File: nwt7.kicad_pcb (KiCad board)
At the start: 2 copper layers, 119.1 x 117.3 mm, 128 parts, among them IC1 PIC16F876A, IC10 AD8307, IC11 MSA0886, IC12 78L10, IC13 AP1117D50, IC15 AP1117D50, IC16 AD8361, IC2 MAX232, IC4 AP1117D50, IC5 AP1117D50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

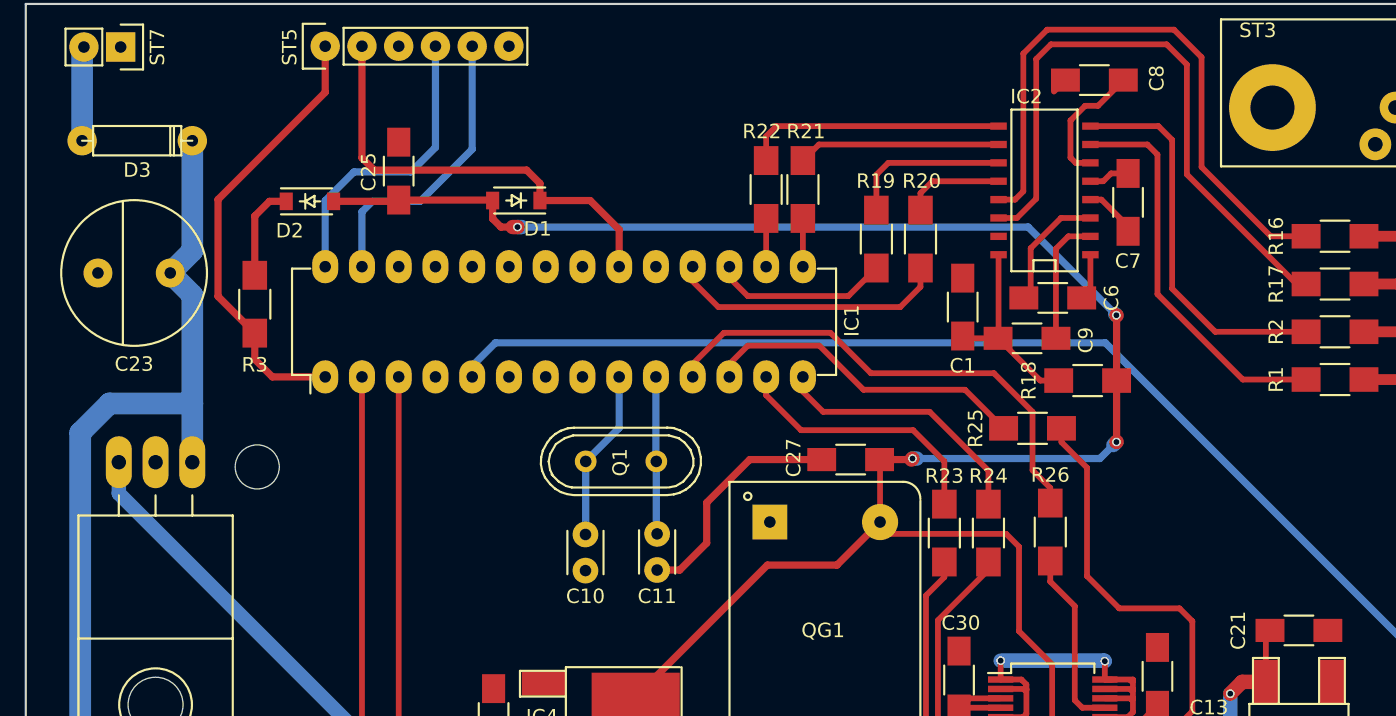
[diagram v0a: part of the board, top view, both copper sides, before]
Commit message: fixed IC3 power
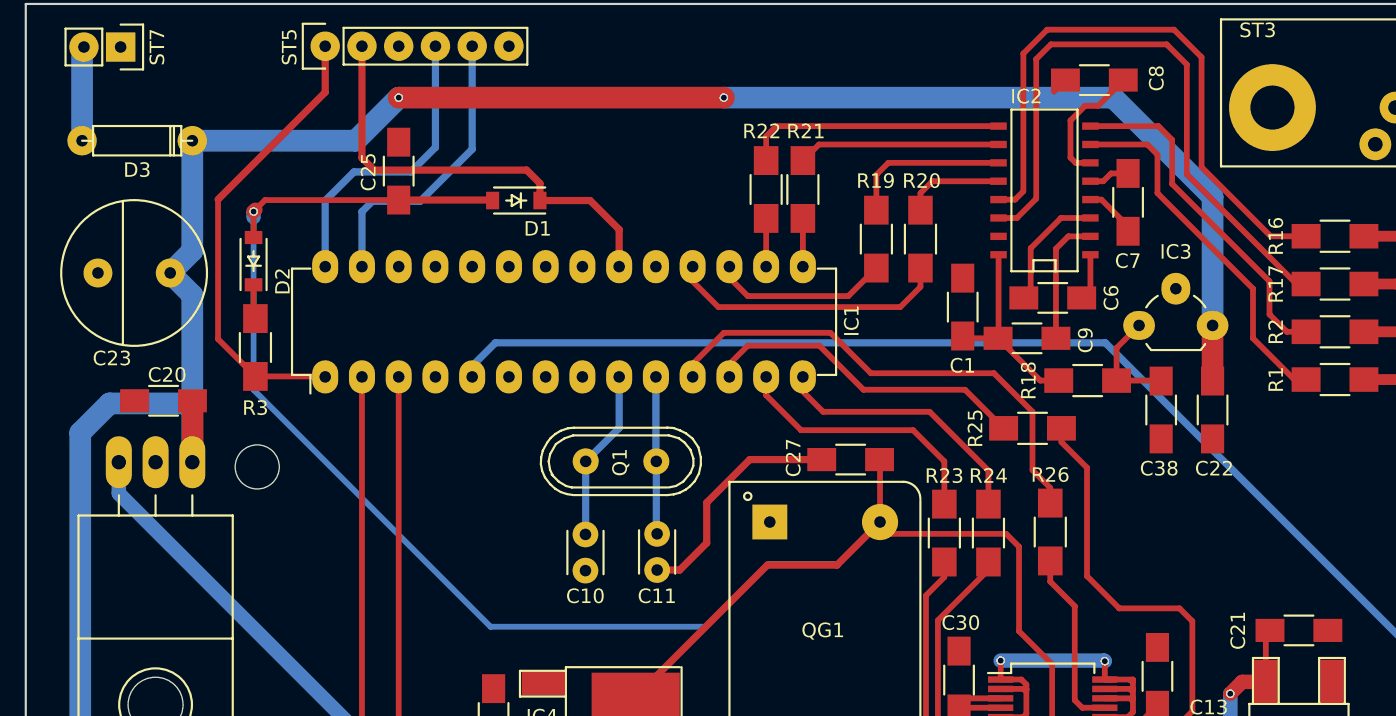
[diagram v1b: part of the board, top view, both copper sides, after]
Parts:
- added C20: 10u, Capacitors_SMD:C_1206_HandSoldering, F.Cu at (21.6, 39.5)
- added C22: 100n, Capacitors_SMD:C_1206_HandSoldering, F.Cu at (94.1, 40.1)
- added C38: 100n, Capacitors_SMD:C_1206_HandSoldering, F.Cu at (90.6, 40.1)
- added IC3: 78L05, TO_SOT_Packages_THT:TO-92_Rugged, F.Cu at (89.0, 34.3)
- moved D2 5.68 mm to (27.8, 29.8), turned to 90 degrees
- moved R3 2.99 mm to (27.9, 35.8)
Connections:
- R18 pad 2: Net-(C25-Pad1) -> Net-(C38-Pad2)
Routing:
- net Net-(C2-Pad2): track 173.7 -> 265.3 mm, vias 0 -> 2
- net Net-(C38-Pad2): track 0.00 -> 7.55 mm
- net Net-(D2-Pad1): track 6.69 -> 2.45 mm
- net Net-(IC2-Pad8): track 26.8 -> 23.9 mm
- net Net-(IC2-Pad7): track 27.3 -> 25.2 mm
- net Net-(IC1-Pad1): track 31.1 -> 31.8 mm
- net Net-(C25-Pad1): track 156.0 -> 156.4 mm, vias 4 -> 1

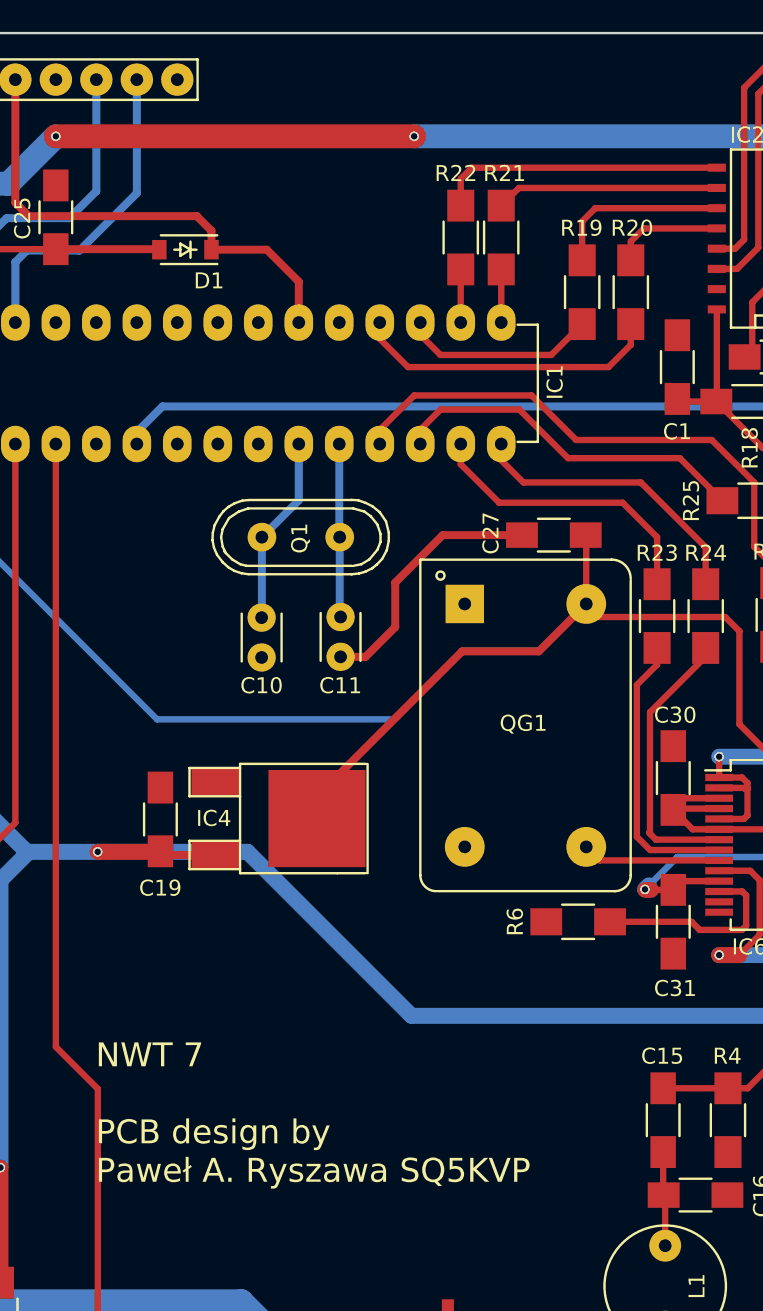
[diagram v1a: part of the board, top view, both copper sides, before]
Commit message: rev. 1.01, added PGM jumper
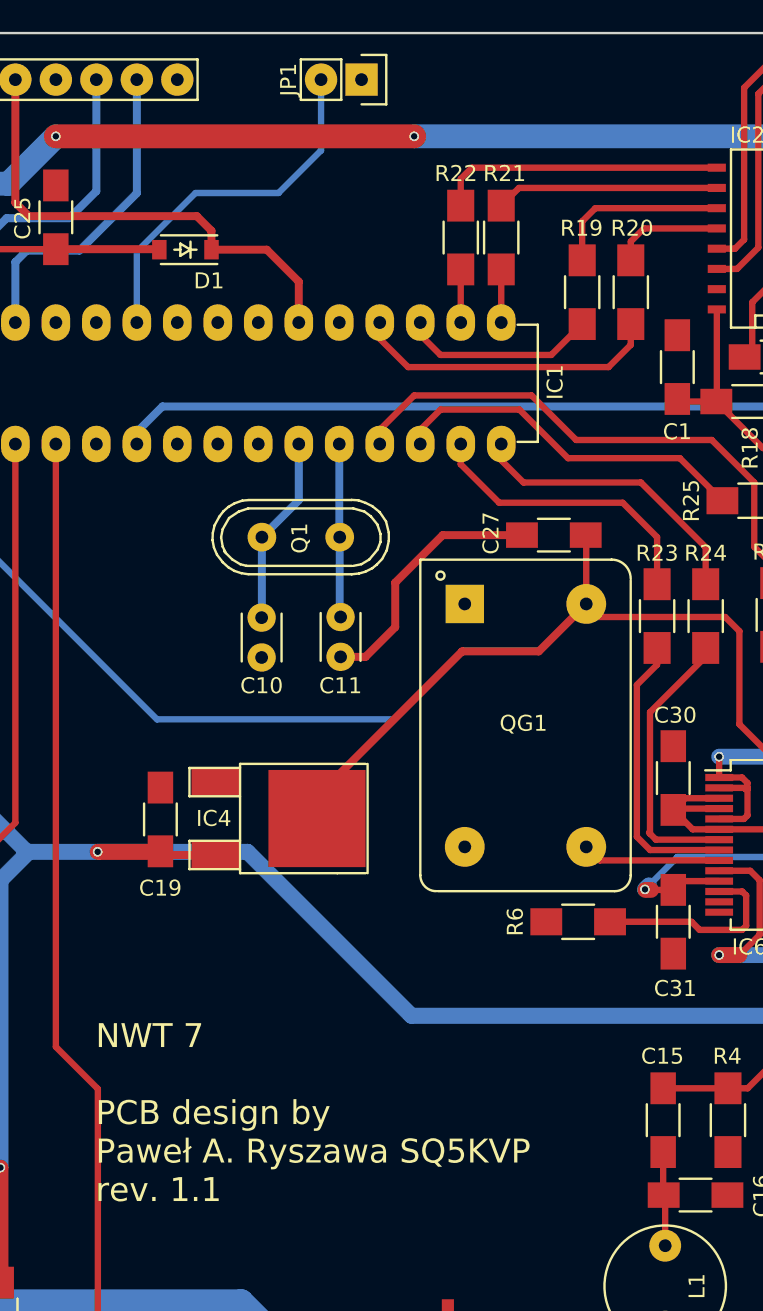
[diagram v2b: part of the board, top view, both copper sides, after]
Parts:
- added JP1: PGM, Pin_Headers:Pin_Header_Straight_1x02, F.Cu at (57.0, 15.0)
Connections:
- IC1 pad 24: (no net) -> Net-(IC1-Pad24)
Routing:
- net Net-(IC1-Pad24): track 0.00 -> 23.1 mm
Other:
- board text added: "NWT 7 PCB design by Paweł A. Ryszawa SQ5KVP rev. 1.1"
- board text removed: "NWT 7 PCB design by Paweł A. Ryszawa SQ5KVP"
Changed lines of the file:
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@@
 (kicad_pcb (version 4) (host pcbnew 4.0.2-stable)
   (general
-    (links 263)
+    (links 265)
     (no_connects 0)
     (area 11.989999 11.989999 131.266001 129.488001)
     (thickness 1.6)
     (drawings 13)
-    (tracks 645)
+    (tracks 650)
     (zones 0)
-    (modules 132)
-    (nets 93)
+    (modules 133)
+    (nets 94)
   )
   (page A4)
@@
   )
   (setup
-    (last_trace_width 1.5)
+    (last_trace_width 0.4)
     (user_trace_width 0.4)
     (user_trace_width 0.5)
@@
     (mod_text_size 1 1)
     (mod_text_width 0.15)
-    (pad_size 2.413 2.413)
+    (pad_size 2.032 2.032)
     (pad_drill 0.8)
     (pad_to_mask_clearance 0.1)
@@
   (net 91 "Net-(C25-Pad1)")
   (net 92 "Net-(C38-Pad2)")
+  (net 93 "Net-(IC1-Pad24)")
   (net_class Default "To jest domyślna klasa połączeń."
     (clearance 0.2)
@@
     (add_net "Net-(IC1-Pad17)")
     (add_net "Net-(IC1-Pad18)")
+    (add_net "Net-(IC1-Pad24)")
     (add_net "Net-(IC1-Pad27)")
     (add_net "Net-(IC1-Pad28)")
@@
     (pad 22 thru_hole oval (at 7.62 15.24 90) (size 2.3 1.8) (drill 0.8) (layers *.Cu *.Mask F.SilkS))
     (pad 23 thru_hole oval (at 7.62 12.7 90) (size 2.3 1.8) (drill 0.8) (layers *.Cu *.Mask F.SilkS))
-    (pad 24 thru_hole oval (at 7.62 10.16 90) (size 2.3 1.8) (drill 0.8) (layers *.Cu *.Mask F.SilkS))
+    (pad 24 thru_hole oval (at 7.62 10.16 90) (size 2.3 1.8) (drill 0.8) (layers *.Cu *.Mask F.SilkS)
+      (net 93 "Net-(IC1-Pad24)"))
     (pad 25 thru_hole oval (at 7.62 7.62 90) (size 2.3 1.8) (drill 0.8) (layers *.Cu *.Mask F.SilkS))
     (pad 26 thru_hole oval (at 7.62 5.08 90) (size 2.3 1.8) (drill 0.8) (layers *.Cu *.Mask F.SilkS))
@@
     )
   )
+  (module Pin_Headers:Pin_Header_Straight_1x02 (layer F.Cu)
+    (at 57.023 14.986 270)
+    (descr "Through hole pin header")
+    (tags "pin header")
+    (fp_text reference JP1 (at 0 4.572 270) (layer F.SilkS)
+      (effects (font (size 1 1) (thickness 0.15)))
+    )
+    (fp_text value PGM (at -0.127 -2.667 270) (layer F.Fab)
+      (effects (font (size 1 1) (thickness 0.15)))
+    )
+    (fp_line (start 1.27 1.27) (end 1.27 3.81) (layer F.SilkS) (width 0.15))
+    (fp_line (start 1.55 -1.55) (end 1.55 0) (layer F.SilkS) (width 0.15))
+    (fp_line (start -1.75 -1.75) (end -1.75 4.3) (layer F.CrtYd) (width 0.05))
+    (fp_line (start 1.75 -1.75) (end 1.75 4.3) (layer F.CrtYd) (width 0.05))
+    (fp_line (start -1.75 -1.75) (end 1.75 -1.75) (layer F.CrtYd) (width 0.05))
+    (fp_line (start -1.75 4.3) (end 1.75 4.3) (layer F.CrtYd) (width 0.05))
+    (fp_line (start 1.27 1.27) (end -1.27 1.27) (layer F.SilkS) (width 0.15))
+    (fp_line (start -1.55 0) (end -1.55 -1.55) (layer F.SilkS) (width 0.15))
+    (fp_line (start -1.55 -1.55) (end 1.55 -1.55) (layer F.SilkS) (width 0.15))
+    (fp_line (start -1.27 1.27) (end -1.27 3.81) (layer F.SilkS) (width 0.15))
+    (fp_line (start -1.27 3.81) (end 1.27 3.81) (layer F.SilkS) (width 0.15))
+    (pad 1 thru_hole rect (at 0 0 270) (size 2.032 2.032) (drill 0.8) (layers *.Cu *.Mask F.SilkS)
+      (net 2 GND))
+    (pad 2 thru_hole oval (at 0 2.54 270) (size 2.032 2.032) (drill 0.8) (layers *.Cu *.Mask F.SilkS)
+      (net 93 "Net-(IC1-Pad24)"))
+    (model Pin_Headers.3dshapes/Pin_Header_Straight_1x02.wrl
+      (at (xyz 0 -0.05 0))
+      (scale (xyz 1 1 1))
+      (rotate (xyz 0 0 90))
+    )
+  )
   (dimension 110.109 (width 0.3) (layer Dwgs.User)
     (gr_text "110.109 mm" (at 142.955 67.1195 270) (layer Dwgs.User)
@@
     (arrow2b (pts (xy 137.922 129.413) (xy 137.335579 128.286496)))
   )
-  (gr_text "NWT 7\n\nPCB design by \nPaweł A. Ryszawa SQ5KVP" (at 40.342 79.812) (layer F.SilkS)
+  (gr_text "NWT 7\n\nPCB design by \nPaweł A. Ryszawa SQ5KVP\nrev. 1.1" (at 40.342 79.812) (layer F.SilkS)
     (effects (font (size 1.5 1.5) (thickness 0.3)) (justify left))
   )
@@
   (segment (start 87.471 38.1) (end 87.471 35.846) (width 0.4) (layer F.Cu) (net 92))
   (segment (start 87.471 35.846) (end 89.027 34.29) (width 0.4) (layer F.Cu) (net 92))
+  (segment (start 42.926 30.226) (end 42.926 25.781) (width 0.4) (layer B.Cu) (net 93))
+  (segment (start 54.483 19.431) (end 54.483 14.986) (width 0.4) (layer B.Cu) (net 93))
+  (segment (start 51.816 22.098) (end 54.483 19.431) (width 0.4) (layer B.Cu) (net 93))
+  (segment (start 46.609 22.098) (end 51.816 22.098) (width 0.4) (layer B.Cu) (net 93))
+  (segment (start 42.926 25.781) (end 46.609 22.098) (width 0.4) (layer B.Cu) (net 93))
   (zone (net 0) (net_name "") (layer F.Cu) (hatch edge 0.508)
     (connect_pads (clearance 0.508))
